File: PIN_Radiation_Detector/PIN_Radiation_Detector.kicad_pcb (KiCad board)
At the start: 2 copper layers, 68.6 x 31.8 mm, 21 parts, among them J1 Conn_01x03, Q1 MMBF4392LT1G, U1 LM358DR

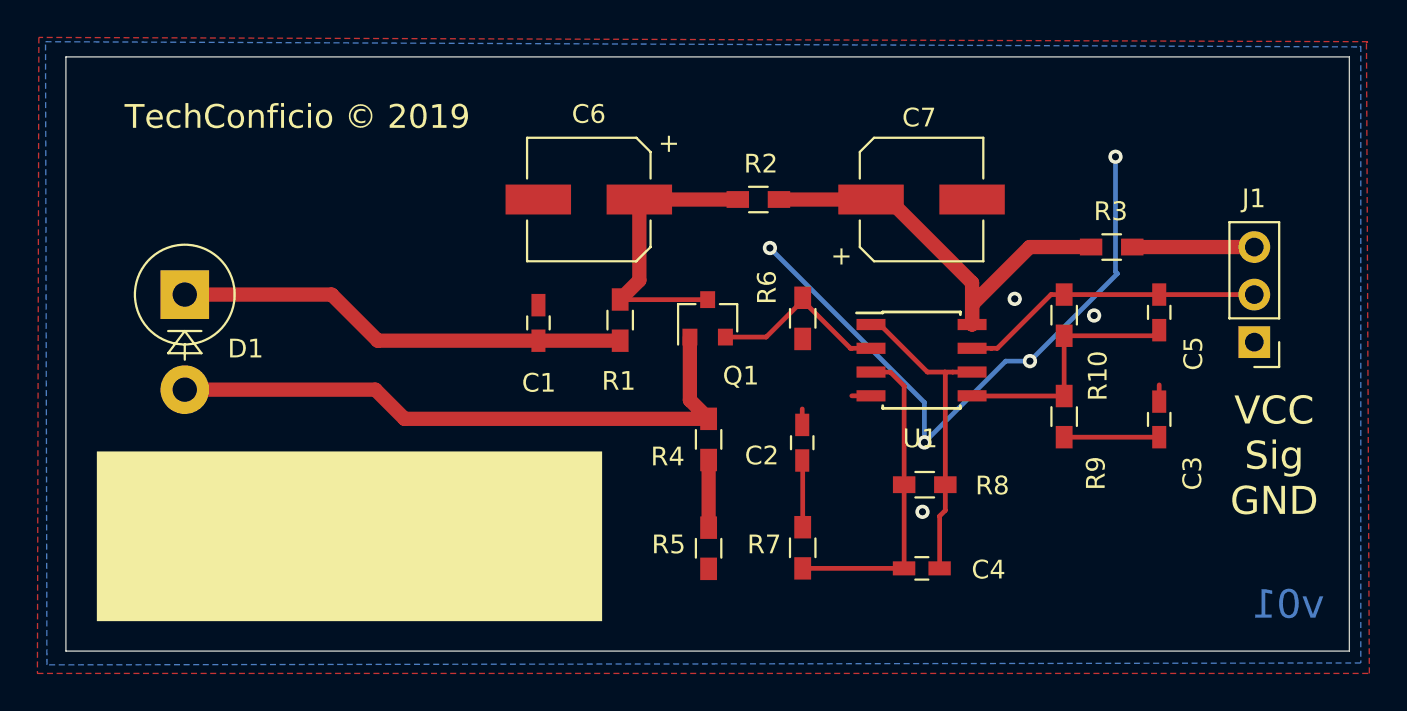
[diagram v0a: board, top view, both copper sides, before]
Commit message: fix stupid op-amp input terminal swap error
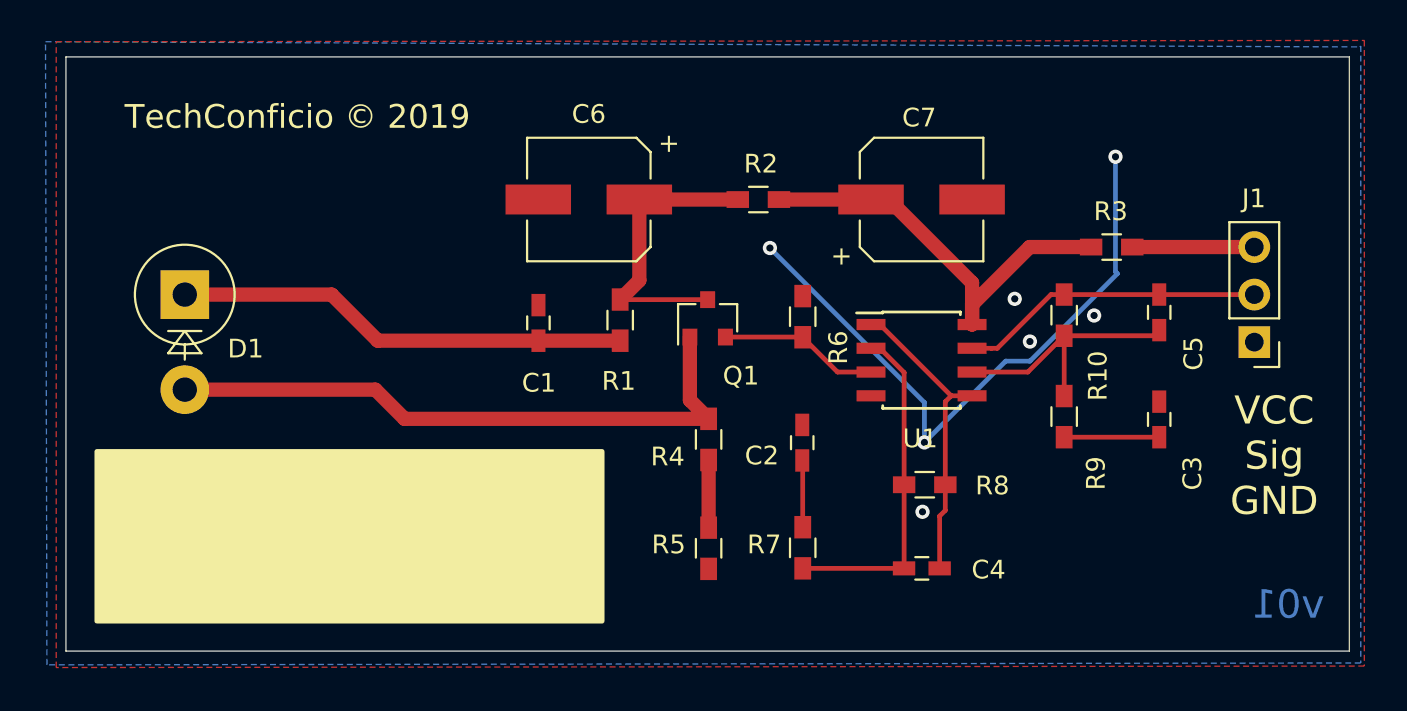
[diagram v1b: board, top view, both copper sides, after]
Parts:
- moved R6 0.09 mm to (181.6, 90.1), turned to -90 degrees
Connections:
- U1 pad 2: Net-(Q1-Pad2) -> Net-(C4-Pad2)
- U1 pad 3: Net-(C4-Pad2) -> Net-(Q1-Pad2)
- U1 pad 5: Net-(C5-Pad2) -> Net-(C4-Pad1)
- U1 pad 6: Net-(C4-Pad1) -> Net-(C5-Pad2)
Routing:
- net GND: track 37.3 -> 34.5 mm
- net Net-(Q1-Pad2): track 9.79 -> 8.55 mm
- net Net-(J1-Pad3): track 7.72 -> 6.52 mm
- net Net-(C6-Pad1): track 16.8 -> 15.7 mm
- net Net-(C4-Pad1): track 17.6 -> 16.5 mm
- net Net-(C4-Pad2): track 17.2 -> 18.2 mm
- net Net-(R4-Pad1): track 4.47 -> 3.62 mm
- net Net-(C5-Pad2): track 13.3 -> 14.1 mm
